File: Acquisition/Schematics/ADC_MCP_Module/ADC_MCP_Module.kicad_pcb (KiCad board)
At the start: 2 copper layers, 18 x 26.8 mm, 30 parts, among them J1 Can, J2 AudioJack4_SwitchTR1, J3 Conn_02x06_Counter_Clockwise, Q1 IRLML9301, SW1 SW_DIP_x01

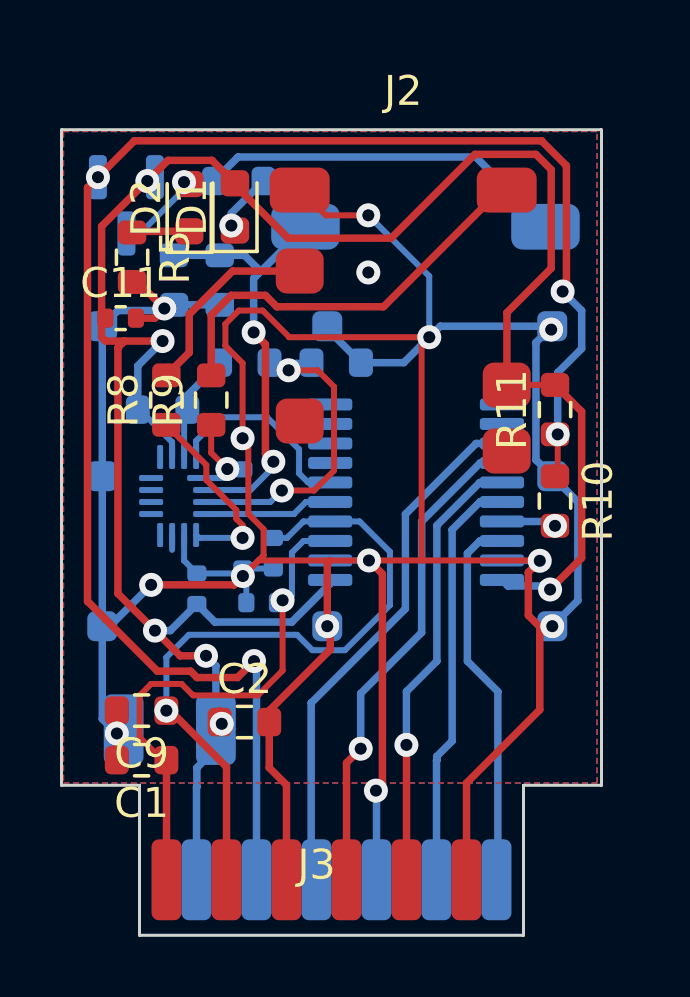
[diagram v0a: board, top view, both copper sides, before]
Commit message: Schematics - FPGA board seems done
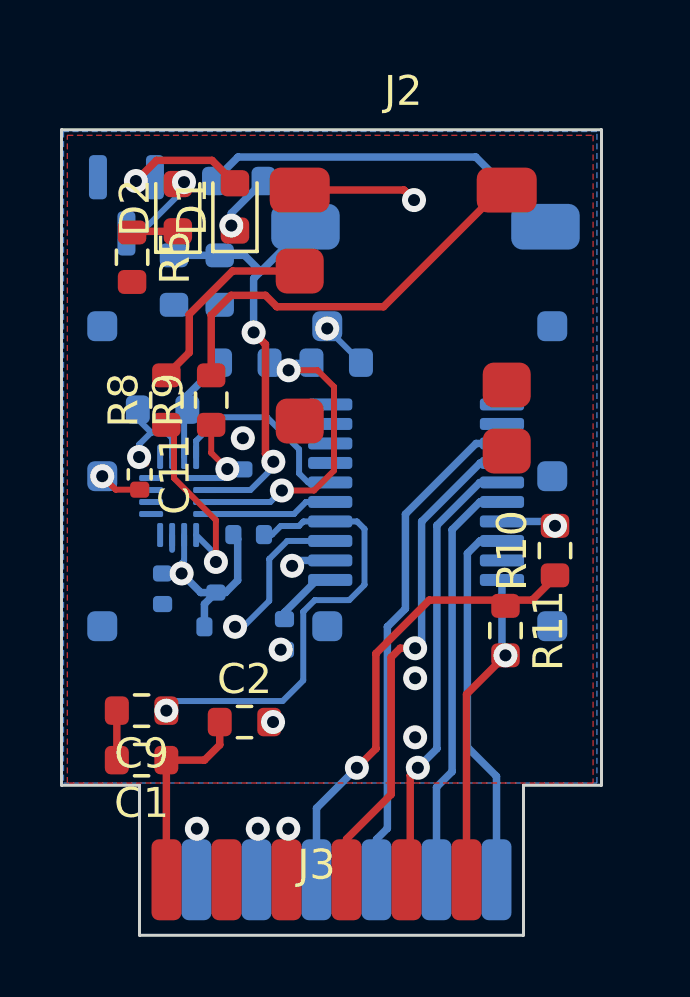
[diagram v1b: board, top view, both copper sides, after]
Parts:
- C7: value 47u -> 100n; footprint Capacitor_Tantalum_SMD:CP_EIA-3528-21_Kemet-B -> Resistor_SMD:R_0402_1005Metric
- moved R11 7.55 mm to (106.3, 91.7), turned to -90 degrees
- moved C11 5.25 mm to (94.1, 86.5), turned to -90 degrees
- moved C7 3.81 mm to (96.8, 91.6)
- moved R10 1.65 mm to (108.0, 89.0), turned to 90 degrees
- moved C8 1.30 mm to (98.9, 91.8), turned to -90 degrees
- moved C5 1.21 mm to (96.6, 89.9)
- moved C3 1.14 mm to (94.9, 90.3)
- moved C10 1.03 mm to (97.7, 88.5), turned to 180 degrees
- moved D2 0.38 mm to (95.4, 77.6)
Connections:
- C1 pad 1: /REFIN- -> /AVdd
- C11 pad 1: +3.3V -> /AVdd
- C2 pad 1: +3.3V -> /AVdd
- C3 pad 1: +3.3V -> /AVdd
- C4 pad 2: GND -> Earth
- C7 pad 1: +3.3V -> Net-(U2-REFIN-)
- C8 pad 1: /REFIN- -> /AVdd
- J2 pad T: +3.3V -> /AVdd
- J3 pad 1: /REFIN- -> /AVdd
- J3 pad 10: /nCS -> /nIRQ
- J3 pad 11: /nIRQ -> Earth
- J3 pad 12: +3.3V -> GND
- J3 pad 3: GND -> Earth
- J3 pad 6: GND -> +3.3V
- J3 pad 9: GND -> /nCS
- R1 pad 2: +3.3V -> /AVdd
- R5 pad 2: GND -> Earth
- R7 pad 2: GND -> Earth
- U1 pad 14: +3.3V -> /AVdd
- U2 pad 1: +3.3V -> /AVdd
- U2 pad 19: GND -> Earth
- U2 pad 3: /REFIN- -> Net-(U2-REFIN-)
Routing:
- net GND: track 131.9 -> 18.3 mm, vias 14 -> 9
- net (no net): track 0.00 -> 82.1 mm
- net +3.3V: track 75.8 -> 15.2 mm, vias 6 -> 2
- net /nIRQ: track 55.9 -> 16.0 mm, vias 4 -> 1
- net /REFIN-: track 17.8 -> 0.00 mm, vias 1 -> 0
- net /AVdd: track 0.00 -> 12.4 mm, vias 0 -> 1
- net /REFIN+: track 23.2 -> 15.3 mm
- net Net-(U2-REFIN-): track 0.00 -> 5.17 mm, vias 0 -> 1
- net Earth: track 0.00 -> 3.45 mm, vias 0 -> 4
- net /nCS: track 17.8 -> 16.8 mm
- added copper zone on F.Cu, net +3.3V
- added copper zone on B.Cu, net /AVdd
- added copper zone on In1.Cu, net Earth
- added copper zone on In1.Cu, net GND
- removed copper zone on B.Cu, net GND
- removed copper zone on F.Cu, net GND
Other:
- copper layers 2 -> 4

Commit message: Acquisition schematics should be working.
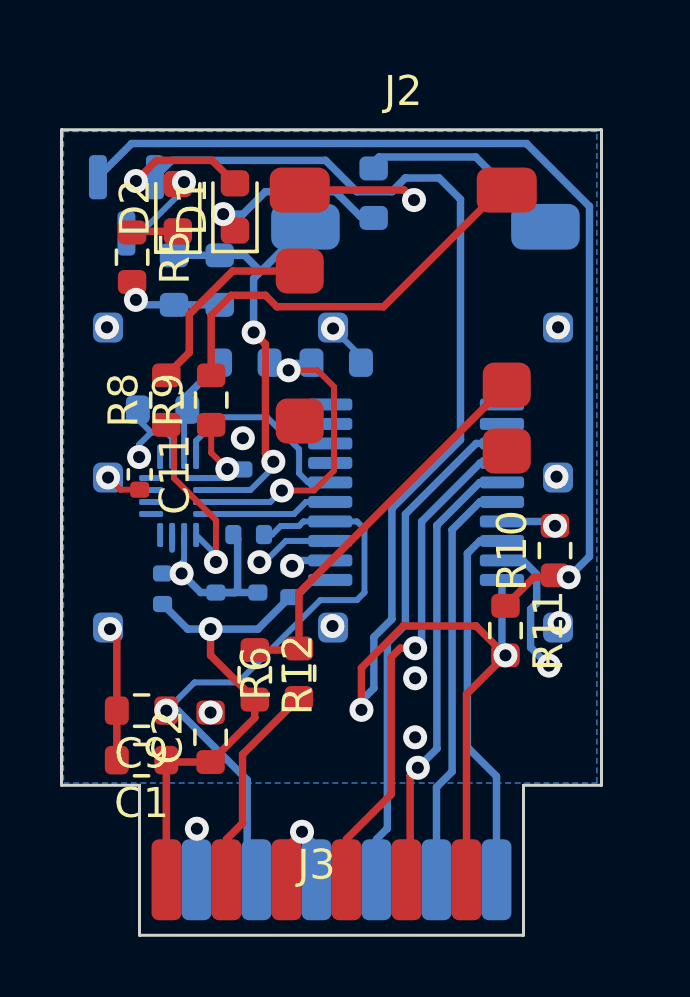
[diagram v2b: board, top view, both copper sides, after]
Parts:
- added R12: 0, Resistor_SMD:R_0603_1608Metric, F.Cu at (97.9, 93.2)
- added R6: 0, Resistor_SMD:R_0603_1608Metric, F.Cu at (99.4, 93.1)
- moved R4 4.51 mm to (101.9, 77.1), turned to 90 degrees
- moved C7 2.08 mm to (98.0, 89.9), turned to -90 degrees
- moved C8 1.76 mm to (99.1, 90.1), turned to 90 degrees
- moved C2 1.24 mm to (96.5, 95.2), turned to 90 degrees
- moved J1 0.20 mm to (100.6, 86.6)
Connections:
- J2 pad T: /AVdd -> Net-(J2-PadT)
- J3 pad 10: /nIRQ -> Earth
- J3 pad 11: Earth -> /REFIN+
- J3 pad 2: /REFIN+ -> +5VA
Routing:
- net (no net): track 82.1 -> 0.00 mm
- net +3.3V: track 15.2 -> 52.1 mm, vias 2 -> 3
- net /nIRQ: track 16.0 -> 32.9 mm
- net Net-(J2-PadT): track 0.00 -> 13.1 mm
- net /AVdd: track 12.4 -> 21.1 mm, vias 1 -> 2
- net Earth: track 3.45 -> 11.5 mm, vias 4 -> 5
- net +5VA: track 0.00 -> 7.06 mm
- net /REFIN+: track 15.3 -> 21.2 mm
- net Net-(R4-Pad2): track 12.3 -> 6.98 mm
- net Net-(D1-K): track 2.15 -> 6.22 mm
- net GND: track 18.3 -> 21.4 mm, vias 9 -> 14
- net Net-(U2-REFIN-): track 5.17 -> 2.65 mm
- added copper zone on In2.Cu, net Earth
- added copper zone on In2.Cu, net GND
- removed copper zone on F.Cu, net +3.3V

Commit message: PCBs production ready
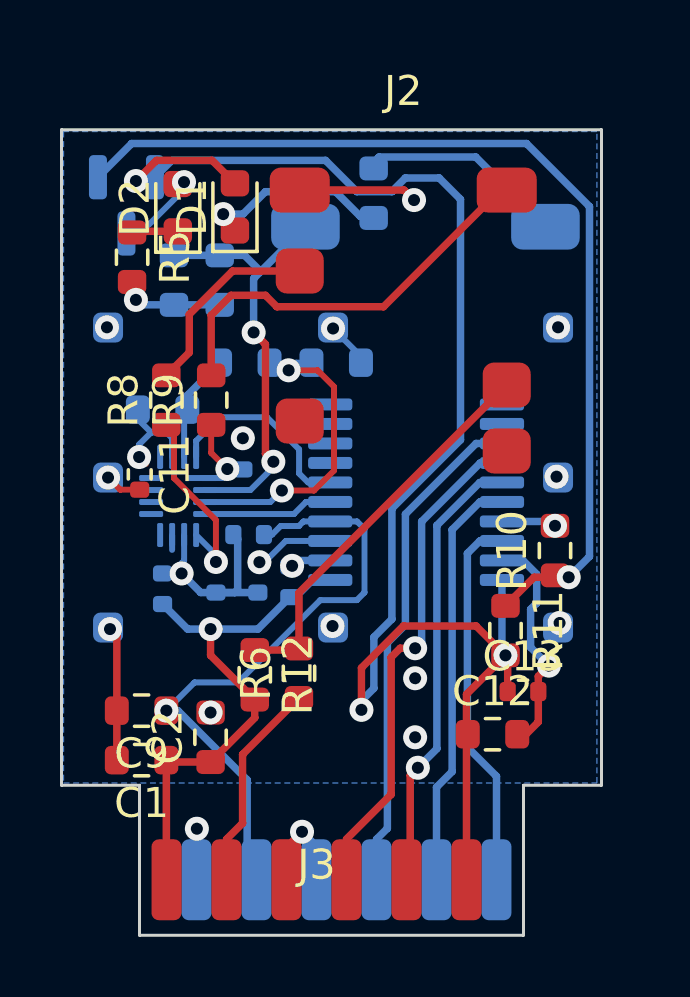
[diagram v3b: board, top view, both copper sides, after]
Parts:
- added C12: 10u, Resistor_SMD:R_0603_1608Metric, F.Cu at (105.9, 95.1)
- added C13: 100n, Resistor_SMD:R_0402_1005Metric, F.Cu at (106.9, 93.7)
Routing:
- net Earth: track 11.5 -> 73.4 mm
- net +3.3V: track 52.1 -> 53.3 mm
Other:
- board text added: "1."
- board text added: "BFM"
- board text added: "C"
- board text added: "IRQ"
- board text added: "ΔΣ"
